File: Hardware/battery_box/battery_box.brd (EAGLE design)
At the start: 60 x 80.1 mm, 44 parts, among them IC1 AD826R, J1 CON_HEADER_PRG_PIC_ICSPA, Q1 IRFR5505PBFTO252, Q2 BSS123, X1 CON_MOLEX_39_29_1028, X2 KUSBVX

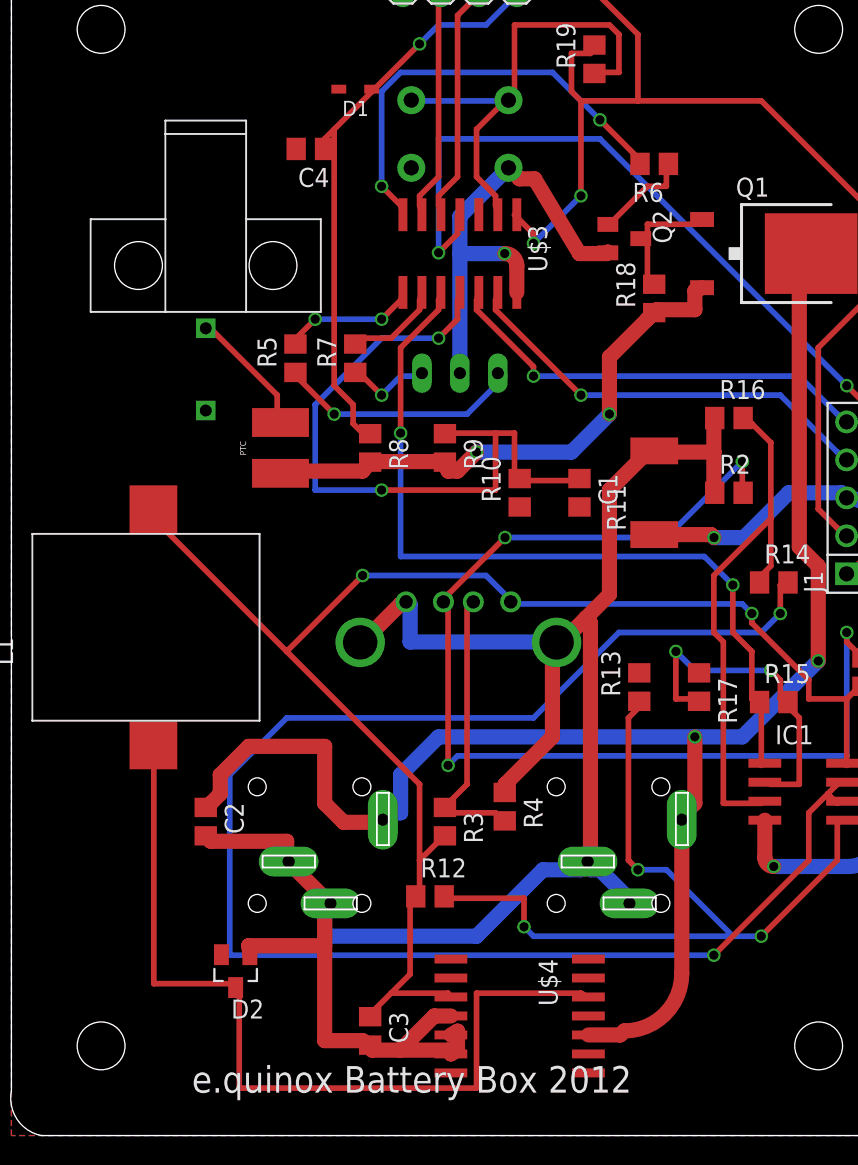
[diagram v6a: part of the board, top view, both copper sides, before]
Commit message: Updated the DC Jack and Battery Connector
Fixed problems with footprints
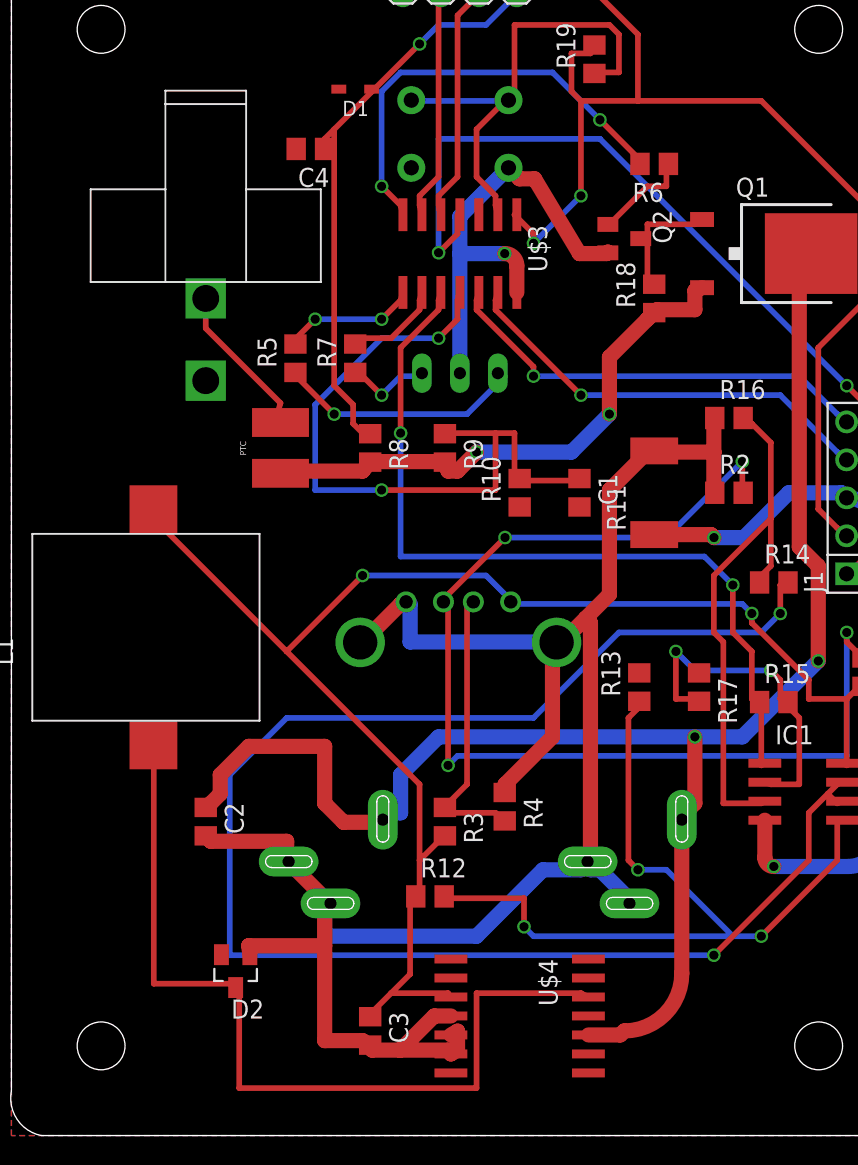
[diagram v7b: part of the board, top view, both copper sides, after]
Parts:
- added U$1: EQUINOX_LOGO_SMALL, equinox:EQUINOX_LOGO_SMALL
- moved X1 2.00 mm to (13.0, 56.0)
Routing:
- net N$6: track 8.49 -> 10.4 mm
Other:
- board text added: "Cap C2 needs to be closer to the LM2574"
- board text added: "e.quinox Battery Box 2013"
- board text removed: "e.quinox Battery Box 2012"
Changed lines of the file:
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@@
 <?xml version="1.0" encoding="utf-8"?>
 <!DOCTYPE eagle SYSTEM "eagle.dtd">
-<eagle version="6.4">
+<eagle version="6.3">
 <drawing>
 <settings>
@@
 <layers>
 <layer number="1" name="Top" color="4" fill="1" visible="yes" active="yes"/>
+<layer number="2" name="Route2" color="1" fill="3" visible="no" active="no"/>
+<layer number="3" name="Route3" color="4" fill="3" visible="no" active="no"/>
+<layer number="4" name="Route4" color="1" fill="4" visible="no" active="no"/>
+<layer number="5" name="Route5" color="4" fill="4" visible="no" active="no"/>
+<layer number="6" name="Route6" color="1" fill="8" visible="no" active="no"/>
+<layer number="7" name="Route7" color="4" fill="8" visible="no" active="no"/>
+<layer number="8" name="Route8" color="1" fill="2" visible="no" active="no"/>
+<layer number="9" name="Route9" color="4" fill="2" visible="no" active="no"/>
+<layer number="10" name="Route10" color="1" fill="7" visible="no" active="no"/>
+<layer number="11" name="Route11" color="4" fill="7" visible="no" active="no"/>
+<layer number="12" name="Route12" color="1" fill="5" visible="no" active="no"/>
+<layer number="13" name="Route13" color="4" fill="5" visible="no" active="no"/>
+<layer number="14" name="Route14" color="1" fill="6" visible="no" active="no"/>
+<layer number="15" name="Route15" color="4" fill="6" visible="no" active="no"/>
 <layer number="16" name="Bottom" color="1" fill="1" visible="yes" active="yes"/>
 <layer number="17" name="Pads" color="2" fill="1" visible="yes" active="yes"/>
@@
 <layer number="46" name="Milling" color="3" fill="1" visible="yes" active="yes"/>
 <layer number="47" name="Measures" color="7" fill="1" visible="no" active="yes"/>
-<layer number="48" name="Document" color="7" fill="1" visible="no" active="yes"/>
+<layer number="48" name="Document" color="7" fill="1" visible="yes" active="yes"/>
 <layer number="49" name="Reference" color="7" fill="1" visible="no" active="yes"/>
 <layer number="50" name="dxf" color="7" fill="1" visible="no" active="no"/>
@@
 <board>
 <plain>
-<text x="12.07" y="2.87" size="1.778" layer="25" font="vector">e.quinox Battery Box 2012</text>
+<text x="41.93" y="1.87" size="1.778" layer="26" font="vector" rot="MR0">e.quinox Battery
+Box 2013</text>
 <wire x1="0" y1="3" x2="0" y2="79" width="0" layer="20"/>
 <wire x1="2" y1="80" x2="58" y2="80" width="0" layer="20"/>
@@
 <wire x1="58" y1="80" x2="60" y2="78" width="0" layer="20" curve="-90"/>
 <wire x1="0" y1="79" x2="2" y2="80" width="0" layer="20" curve="-90"/>
-<dimension x1="60" y1="80" x2="60" y2="0" x3="69" y3="40" textsize="3.5" layer="51"/>
-<dimension x1="0" y1="80" x2="60" y2="80" x3="30" y3="85" textsize="3.5" layer="51"/>
-<dimension x1="20" y1="20.88" x2="0" y2="21" x3="9.78400625" y3="-15.05870625" textsize="3.5" layer="51"/>
-<dimension x1="20" y1="20.88" x2="40" y2="20.88" x3="30" y3="-15" textsize="3.5" layer="51"/>
-<dimension x1="40" y1="20.88" x2="60" y2="21" x3="50.215775" y3="-15.02270625" textsize="3.5" layer="51"/>
-<dimension x1="6" y1="6" x2="6" y2="0" x3="-5" y3="3" textsize="3.5" layer="51"/>
-<dimension x1="6" y1="6" x2="0" y2="6" x3="3" y3="-6" textsize="3.5" layer="51"/>
-<dimension x1="54" y1="6" x2="54" y2="0" x3="66" y3="3" textsize="3.5" layer="51"/>
-<dimension x1="54" y1="6" x2="60" y2="6" x3="57" y3="-6" textsize="3.5" layer="51"/>
-<dimension x1="30" y1="67" x2="0" y2="67" x3="15" y3="98" textsize="3.5" layer="51"/>
-<dimension x1="30" y1="67" x2="30" y2="80" x3="-10" y3="73.5" textsize="3.5" layer="51"/>
-<dimension x1="30" y1="51" x2="30" y2="80" x3="-21" y3="65.5" textsize="3.5" layer="51"/>
-<dimension x1="30" y1="33" x2="30" y2="80" x3="-34" y3="56.5" textsize="3.5" layer="51"/>
+<dimension x1="60" y1="80" x2="60" y2="0" x3="69" y3="40" layer="51"/>
+<dimension x1="0" y1="80" x2="60" y2="80" x3="30" y3="85" layer="51"/>
+<dimension x1="20" y1="20.88" x2="0" y2="21" x3="9.78400625" y3="-15.05870625" layer="51"/>
+<dimension x1="20" y1="20.88" x2="40" y2="20.88" x3="30" y3="-15" layer="51"/>
+<dimension x1="40" y1="20.88" x2="60" y2="21" x3="50.215775" y3="-15.02270625" layer="51"/>
+<dimension x1="6" y1="6" x2="6" y2="0" x3="-5" y3="3" layer="51"/>
+<dimension x1="6" y1="6" x2="0" y2="6" x3="3" y3="-6" layer="51"/>
+<dimension x1="54" y1="6" x2="54" y2="0" x3="66" y3="3" layer="51"/>
+<dimension x1="54" y1="6" x2="60" y2="6" x3="57" y3="-6" layer="51"/>
+<dimension x1="30" y1="67" x2="0" y2="67" x3="15" y3="98" layer="51"/>
+<dimension x1="30" y1="67" x2="30" y2="80" x3="-10" y3="73.5" layer="51"/>
+<dimension x1="30" y1="51" x2="30" y2="80" x3="-21" y3="65.5" layer="51"/>
+<dimension x1="30" y1="33" x2="30" y2="80" x3="-34" y3="56.5" layer="51"/>
+<text x="-17" y="18" size="1.778" layer="48">Cap C2 needs to be closer
+to the LM2574</text>
 </plain>
 <attributes>
@@
 <element name="U$7" library="equinox" package="PCBMOUNT" value="PCB_MOUNT_RICHO" x="54" y="74" rot="MR0"/>
 <element name="U$8" library="equinox" package="PCBMOUNT" value="PCB_MOUNT_RICHO" x="6" y="74" rot="MR0"/>
-<element name="X1" library="equinox" package="MOLEX_39_29_1028" value="CON_MOLEX_39_29_1028" x="13" y="54" rot="R180"/>
+<element name="X1" library="equinox" package="MOLEX_39_29_1028" value="CON_MOLEX_39_29_1028" x="13" y="56" rot="R180"/>
 <element name="R1" library="rcl" package="R0805" value="75k" x="57" y="31" rot="R270"/>
 <element name="R2" library="rcl" package="R0805" value="49.9k" x="48" y="43"/>
@@
 <attribute name="OC_FARNELL" value="unknown" x="30" y="77" size="1.778" layer="27" display="off"/>
 </element>
+<element name="U$1" library="equinox" package="EQUINOX_LOGO_SMALL" value="EQUINOX_LOGO_SMALL" x="47" y="57" rot="MR0"/>
 </elements>
 <signals>
@@
 <contactref element="U$2" pad="P$1"/>
 <contactref element="X1" pad="P$1"/>
-<wire x1="17.78" y1="49.53" x2="13.335" y2="53.975" width="0.381" layer="1"/>
-<wire x1="17.78" y1="48.26" x2="17.78" y2="49.53" width="0.381" layer="1"/>
-<wire x1="13.335" y1="53.975" x2="13" y2="54" width="0.381" layer="1"/>
+<wire x1="18" y1="49" x2="13" y2="54" width="0.381" layer="1"/>
+<wire x1="17.78" y1="48.26" x2="18" y2="49" width="0.381" layer="1"/>
+<wire x1="13" y1="54" x2="13" y2="56" width="0.381" layer="1"/>
 <wire x1="17.78" y1="48.26" x2="18" y2="47.7" width="0.381" layer="1"/>
 </signal>
@@
 </signal>
 </signals>
-<errors>
-</errors>
 </board>
 </drawing>
+<compatibility>
+<note version="6.3" minversion="6.2.2" severity="warning">
+Since Version 6.2.2 text objects can contain more than one line,
+which will not be processed correctly with this version.
+</note>
+</compatibility>
 </eagle>

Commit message: Changed Current Sense Resistor Values
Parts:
- R11: value 0.005 -> 0.1
- R16, R17: value 1k -> 20k
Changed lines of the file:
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@@
 <element name="R6" library="rcl" package="R0805" value="1k" x="43" y="65" rot="R180"/>
 <element name="C4" library="rcl" package="C0805" value="22u" x="20" y="66" rot="R180"/>
-<element name="R11" library="rcl" package="R2512" value="0.005" x="43" y="43" rot="R90"/>
+<element name="R11" library="rcl" package="R2512" value="0.1" x="43" y="43" rot="R90"/>
 <element name="IC1" library="analog-devices" package="SO8" value="AD826R" x="53" y="23" rot="R270"/>
 <element name="R12" library="rcl" package="R0805" value="100k" x="28" y="16"/>
@@
 <element name="R14" library="rcl" package="R0805" value="66k" x="51" y="37"/>
 <element name="R15" library="rcl" package="R0805" value="66k" x="51" y="29"/>
-<element name="R16" library="rcl" package="R0805" value="1k" x="48" y="48"/>
-<element name="R17" library="rcl" package="R0805" value="1k" x="46" y="30" rot="R270"/>
+<element name="R16" library="rcl" package="R0805" value="20k" x="48" y="48"/>
+<element name="R17" library="rcl" package="R0805" value="20k" x="46" y="30" rot="R270"/>
 <element name="R18" library="rcl" package="R0805" value="1M" x="43" y="56" rot="R90"/>
 <element name="R19" library="rcl" package="R0805" value="10k" x="39" y="72" rot="R90"/>
